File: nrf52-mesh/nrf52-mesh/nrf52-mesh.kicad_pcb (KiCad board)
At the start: 2 copper layers, 63 parts, among them J1 Conn_02x05_Odd_Even, J2 Conn_01x04_Male, J3 Conn_01x08, U1 TLV62568DBV, U2 MAX1555, U3 FAN5341, U4 TPS560200, U5 BL652, U6 CP2102N-A01-GQFN24, X1 USBFCI_10103594

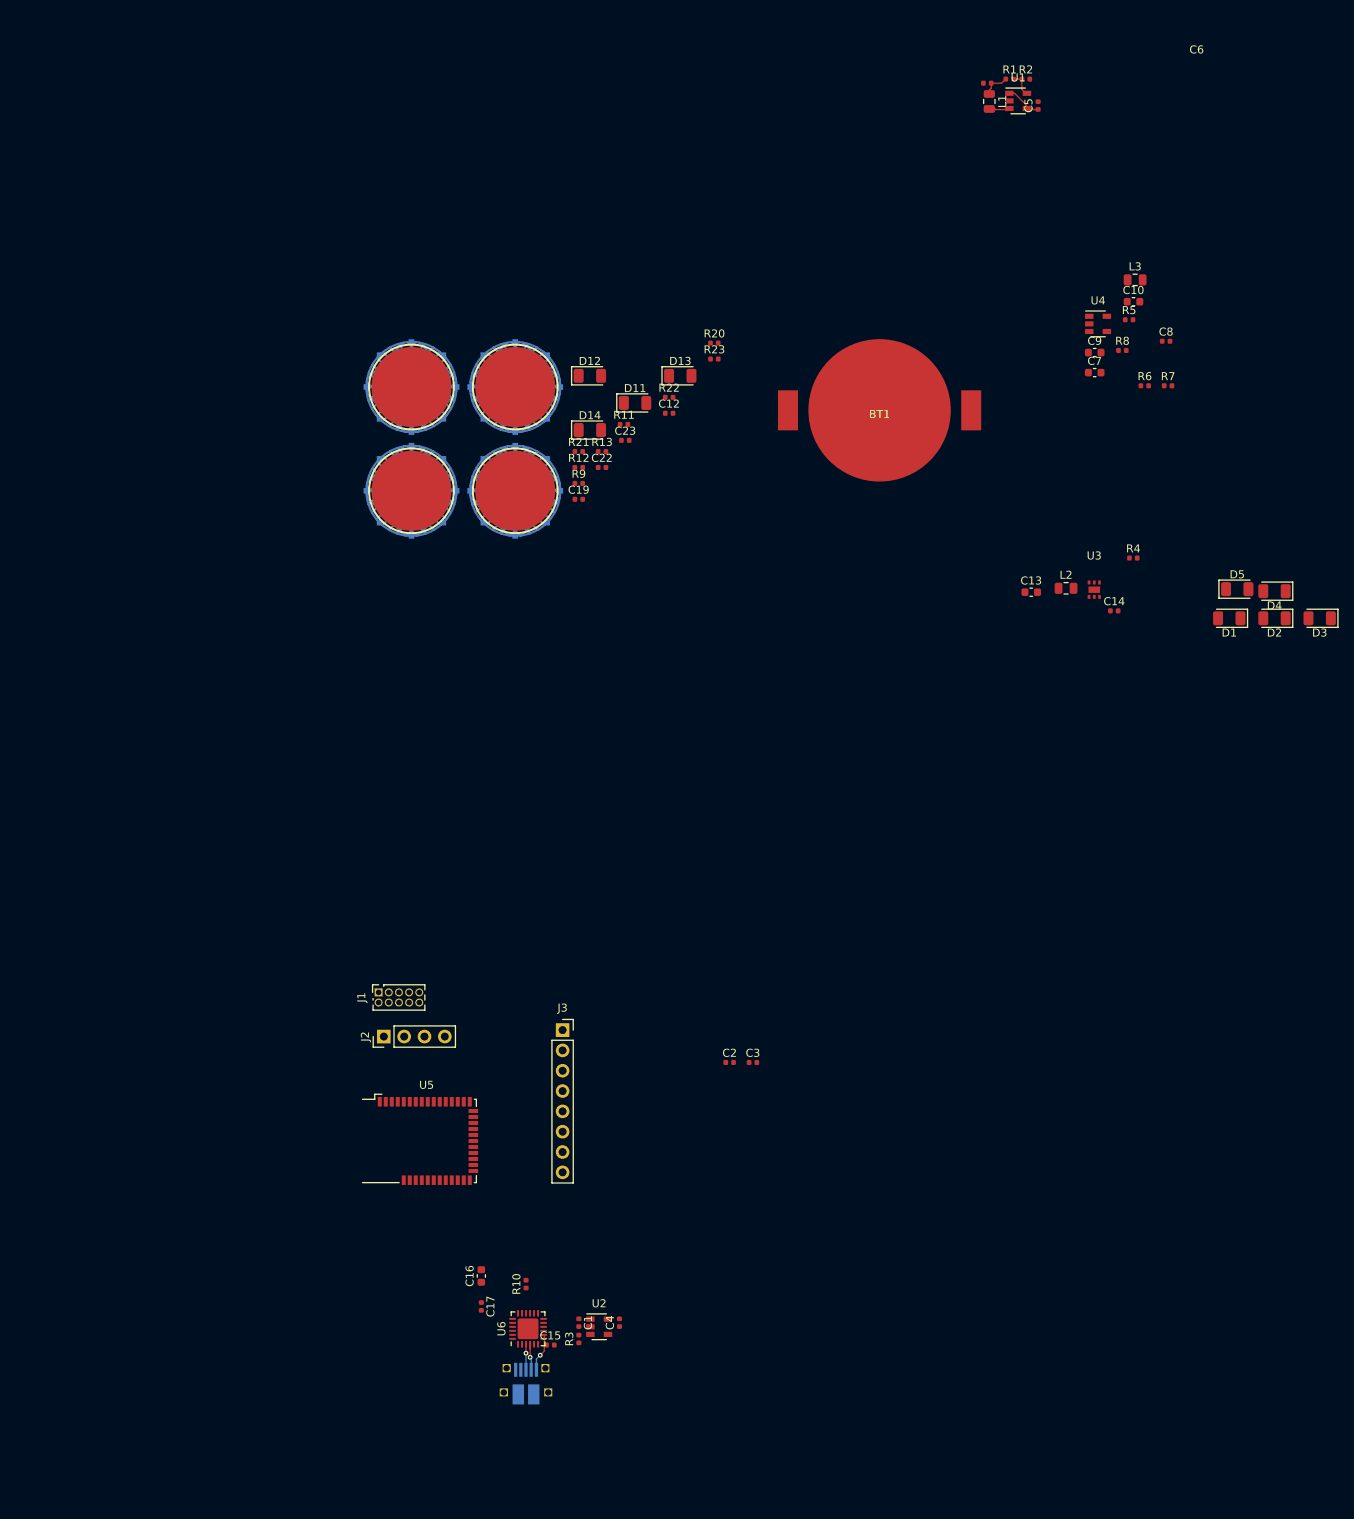
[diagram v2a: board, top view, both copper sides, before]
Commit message: CP2102N + MAX1555 + FAN5341 + TPS560200 + TLV62568
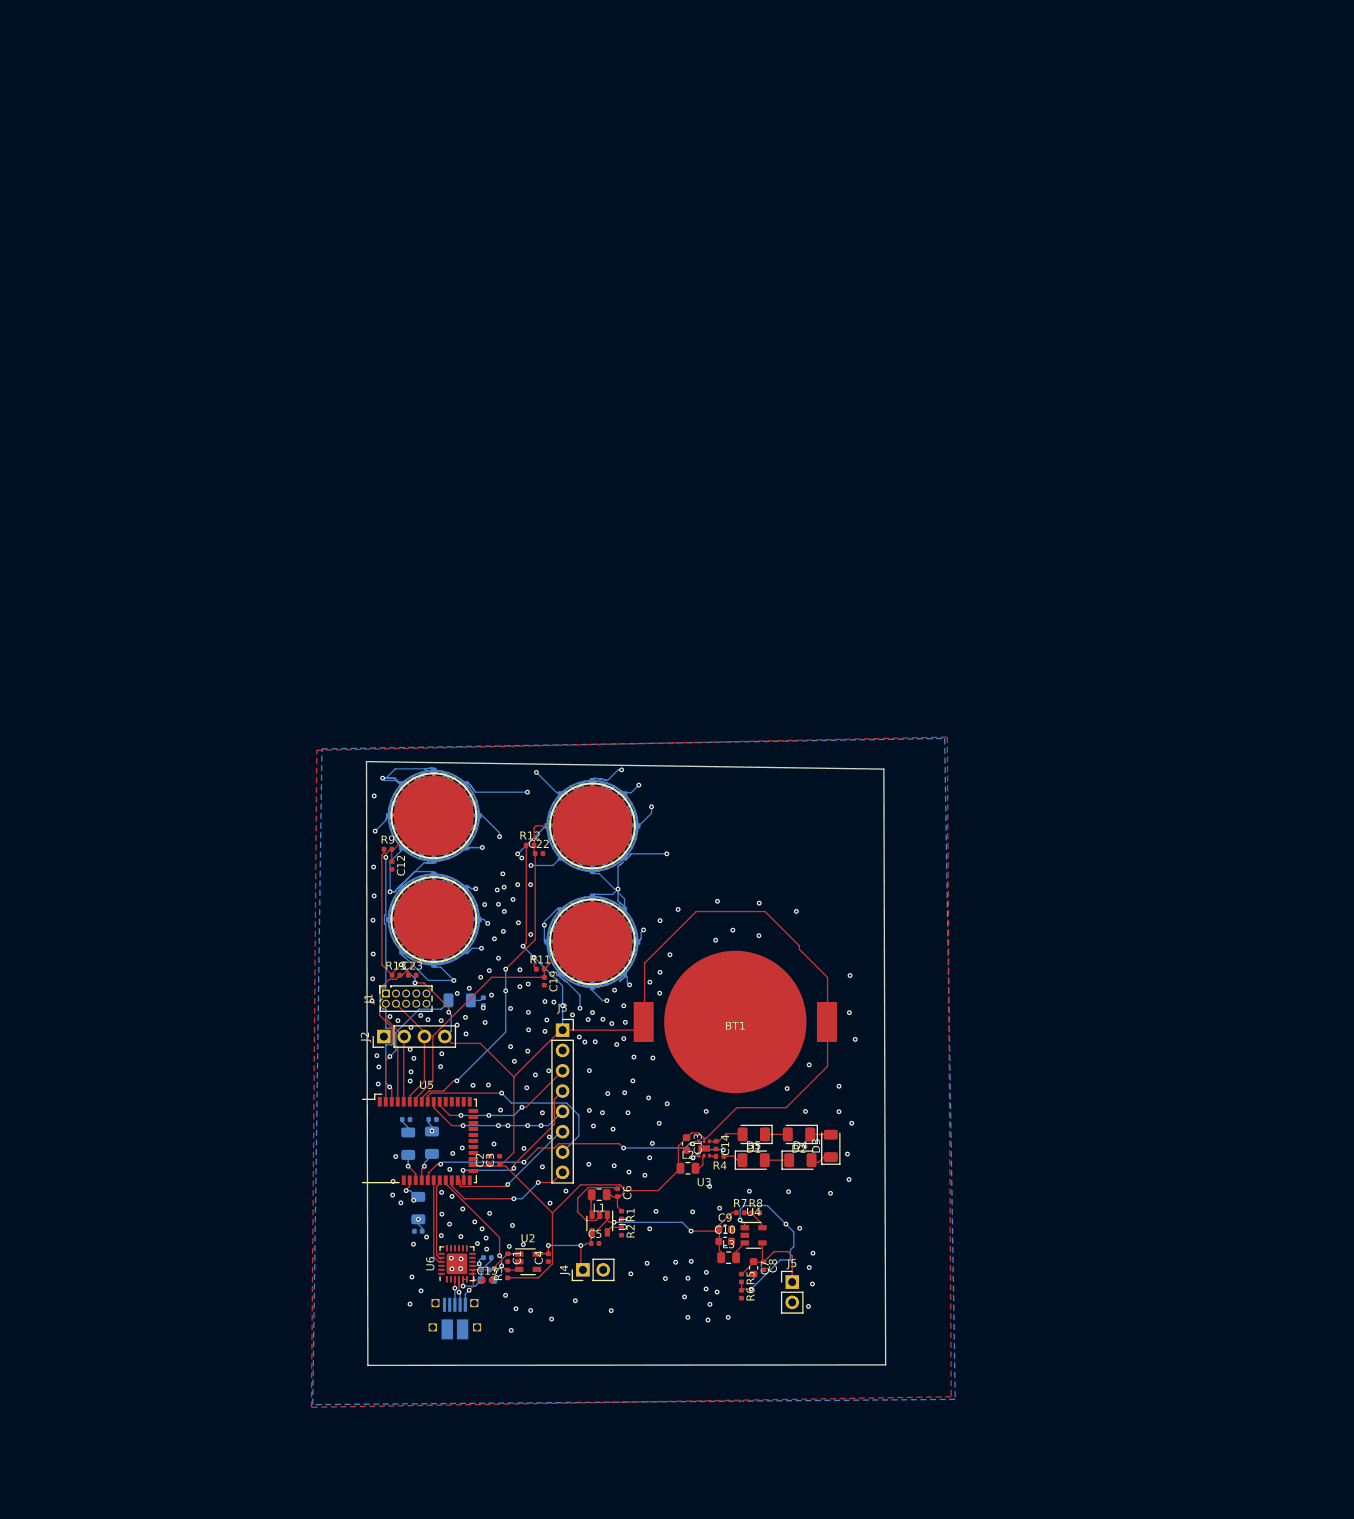
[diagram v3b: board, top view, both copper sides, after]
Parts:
- added J4: Conn_01x02_Male, Connector_PinHeader_2.54mm:PinHeader_1x02_P2.54mm_Vertical, F.Cu at (219.2, 106.9)
- added J5: Conn_01x02_Male, Connector_PinHeader_2.54mm:PinHeader_1x02_P2.54mm_Vertical, F.Cu at (245.4, 108.5)
- C16, C17, D11, D12, D13, D14, R10, R20, R21, R22, R23: moved to B.Cu
- moved C5 152.6 mm to (220.7, 103.6), turned to 0 degrees
- moved R2 152.6 mm to (224.0, 102.1), turned to 270 degrees
- moved R1 150.0 mm to (224.0, 100.1), turned to 270 degrees
- moved U1 149.8 mm to (221.3, 101.1), turned to 270 degrees
- moved C6 146.2 mm to (223.5, 97.3), turned to 90 degrees
- moved L1 145.1 mm to (221.2, 97.5), turned to 180 degrees
- moved L3 132.4 mm to (237.4, 105.4)
- moved R5 129.2 mm to (239.0, 108.0), turned to 270 degrees
- moved C10 128.1 mm to (237.0, 103.4)
- moved C8 126.0 mm to (241.8, 106.4), turned to 270 degrees
- moved R6 124.2 mm to (239.0, 110.0), turned to 270 degrees
- moved U4 121.8 mm to (240.5, 102.6)
- moved C7 119.8 mm to (240.5, 106.7), turned to 270 degrees
- moved C9 118.9 mm to (237.0, 101.9)
- moved R8 117.1 mm to (240.8, 99.8)
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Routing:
- net +3V3: track 3.44 -> 224.1 mm, vias 0 -> 6
- net GND: track 0.00 -> 140.3 mm, vias 0 -> 218
- net CAP4: track 0.00 -> 49.0 mm, vias 0 -> 3
- net CAP1: track 0.00 -> 45.0 mm, vias 0 -> 2
- net LEDREGEN: track 0.00 -> 36.8 mm, vias 0 -> 4
- net CAP3: track 0.00 -> 34.8 mm
- net +5V: track 4.47 -> 37.4 mm, vias 0 -> 4
- net io2: track 0.00 -> 26.3 mm, vias 0 -> 1
- net CAP2: track 0.00 -> 25.2 mm
- net Net-(R5-Pad2): track 0.00 -> 23.1 mm, vias 0 -> 3
- net io5: track 0.00 -> 19.9 mm, vias 0 -> 2
- net io6: track 0.00 -> 18.6 mm, vias 0 -> 3
- net io4: track 0.00 -> 18.5 mm, vias 0 -> 5
- net LED1: track 0.00 -> 17.4 mm, vias 0 -> 1
- net io3: track 0.00 -> 16.7 mm, vias 0 -> 1
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- added copper zone on B.Cu, net GND
- added copper zone on F.Cu, net GND
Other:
- board outline added: 64.9 x 75.5 mm
